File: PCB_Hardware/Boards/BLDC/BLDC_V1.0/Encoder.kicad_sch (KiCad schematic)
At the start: 3 parts, among them U2 MT6835GT-STD

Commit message: Add DBcan transport refactor, BLDC V1.0 schematic + sim work, HAL submodule
- DBcan: replace bare-register driver with vendor-agnostic transport abstraction (core/, transports/, refactored bootloader driver, README)
- Add stm32g4xx_hal_driver as Firmware/libs submodule
- Add HAL config for BLDC board (stm32g4xx_hal_conf.h)
- BLDC V1.0: schematic edits across 10 sheets (footprint assignments, repositioning); design-doc README (gate-driver constraints, FET selection / TPH3R70APL, thermal analysis)
- ngspice simulation workflow (cap sweeps, half-bridge slow turn-on)
- Ignore .obsidian/ vault state and large simulation CSV exports
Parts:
- C1: footprint (none) -> Capacitor_SMD:C_0402_1005Metric
- D1: footprint (none) -> Diode_SMD:D_SOD-323
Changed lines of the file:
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@@
 			)
 		)
-		(property "Footprint" ""
+		(property "Footprint" "Diode_SMD:D_SOD-323"
 			(at 119.38 72.39 0)
 			(hide yes)
@@
 			)
 		)
-		(property "Footprint" ""
+		(property "Footprint" "Capacitor_SMD:C_0402_1005Metric"
 			(at 135.5852 76.2 0)
 			(hide yes)

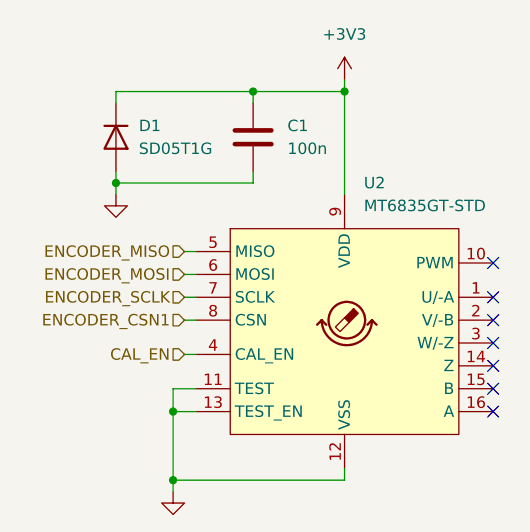
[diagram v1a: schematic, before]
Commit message: Created organization around the symbol lib and did a first pass layout of the BDLC
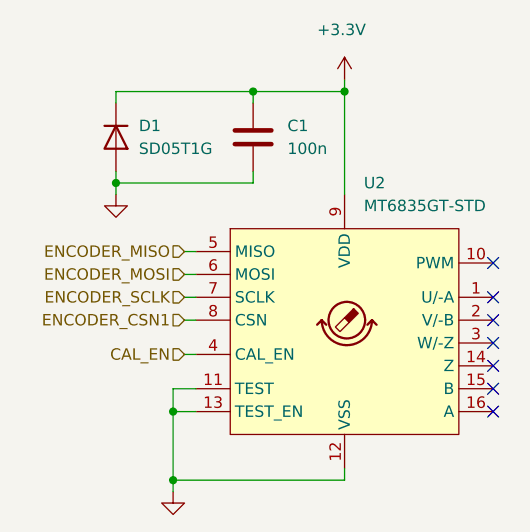
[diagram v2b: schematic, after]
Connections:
- net +3V3 renamed +3.3V
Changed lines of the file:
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@@
 		(in_pos_files yes)
 		(dnp no)
-		(fields_autoplaced yes)
 		(property "Reference" "#PWR03"
 			(at 144.78 69.85 0)
@@
 			)
 		)
-		(property "Value" "+3V3"
-			(at 144.78 60.96 0)
+		(property "Value" "+3.3V"
+			(at 141.732 60.452 0)
 			(show_name no)
 			(do_not_autoplace no)
@@
 					(size 1.27 1.27)
 				)
+				(justify left)
 			)
 		)
